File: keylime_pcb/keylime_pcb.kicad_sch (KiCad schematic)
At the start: 0 parts

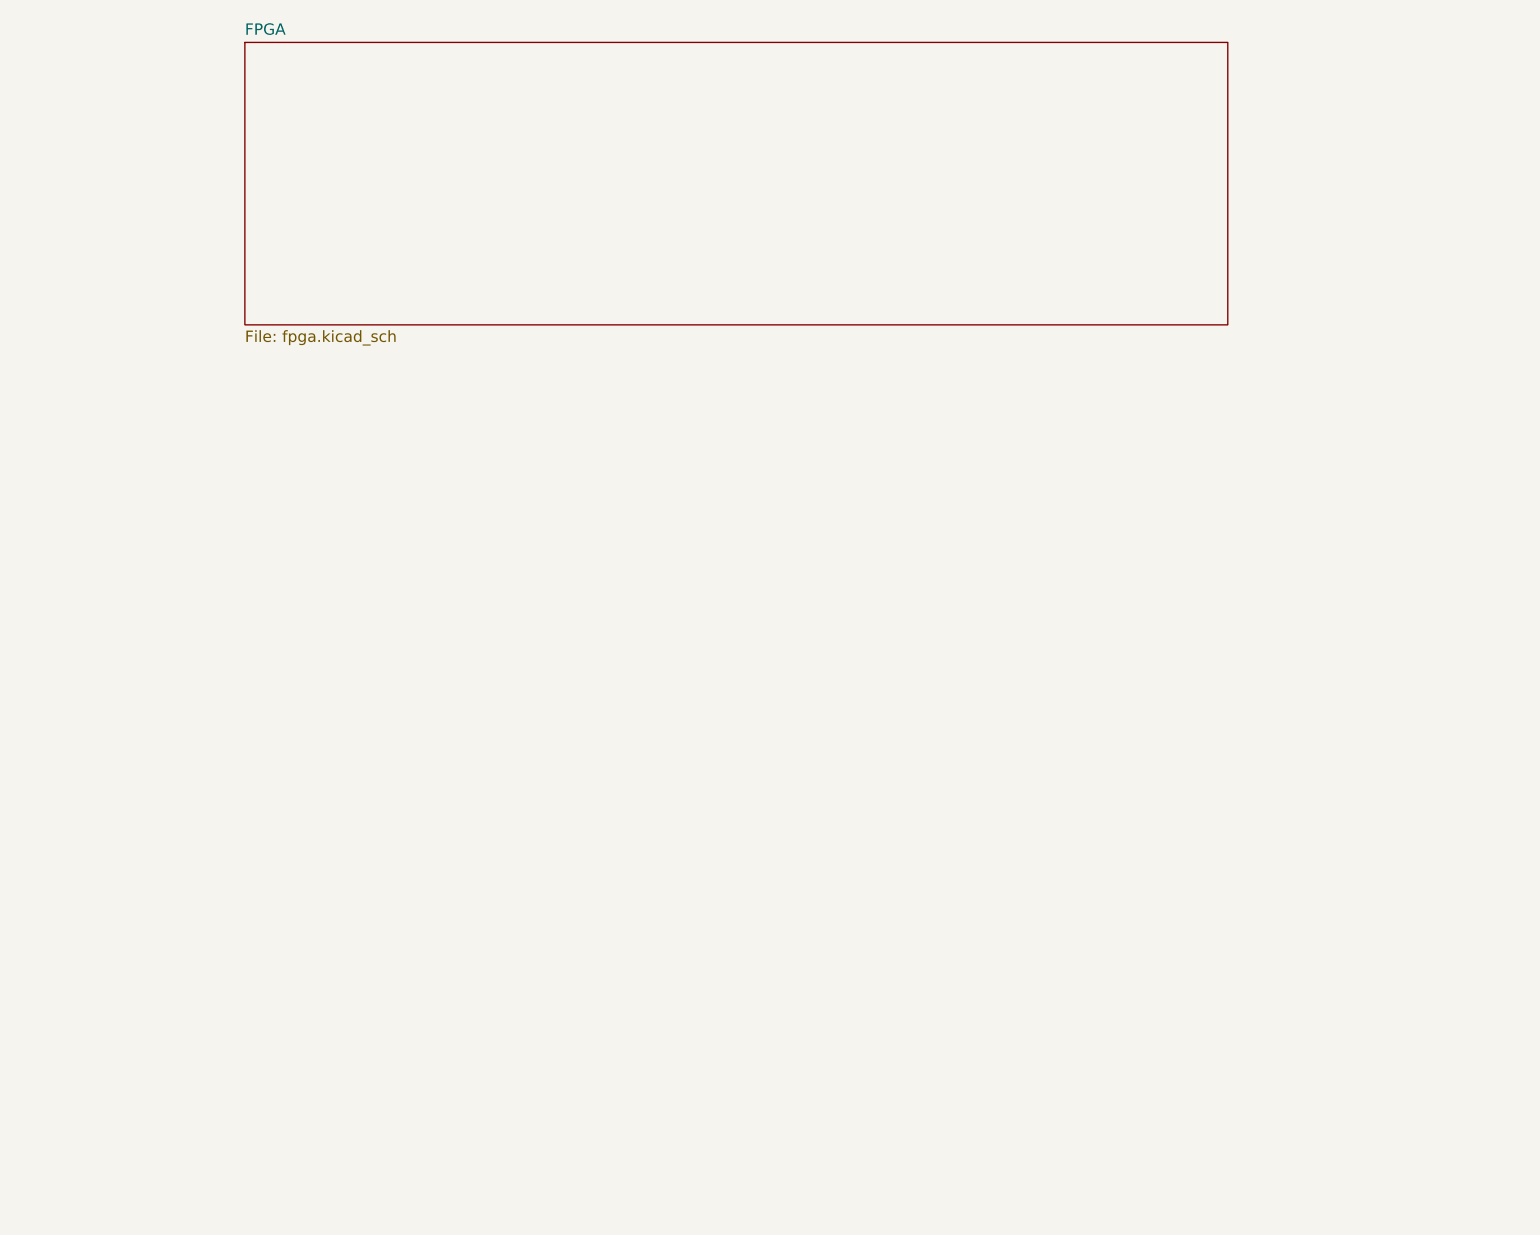
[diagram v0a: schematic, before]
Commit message: Finished adding most components.
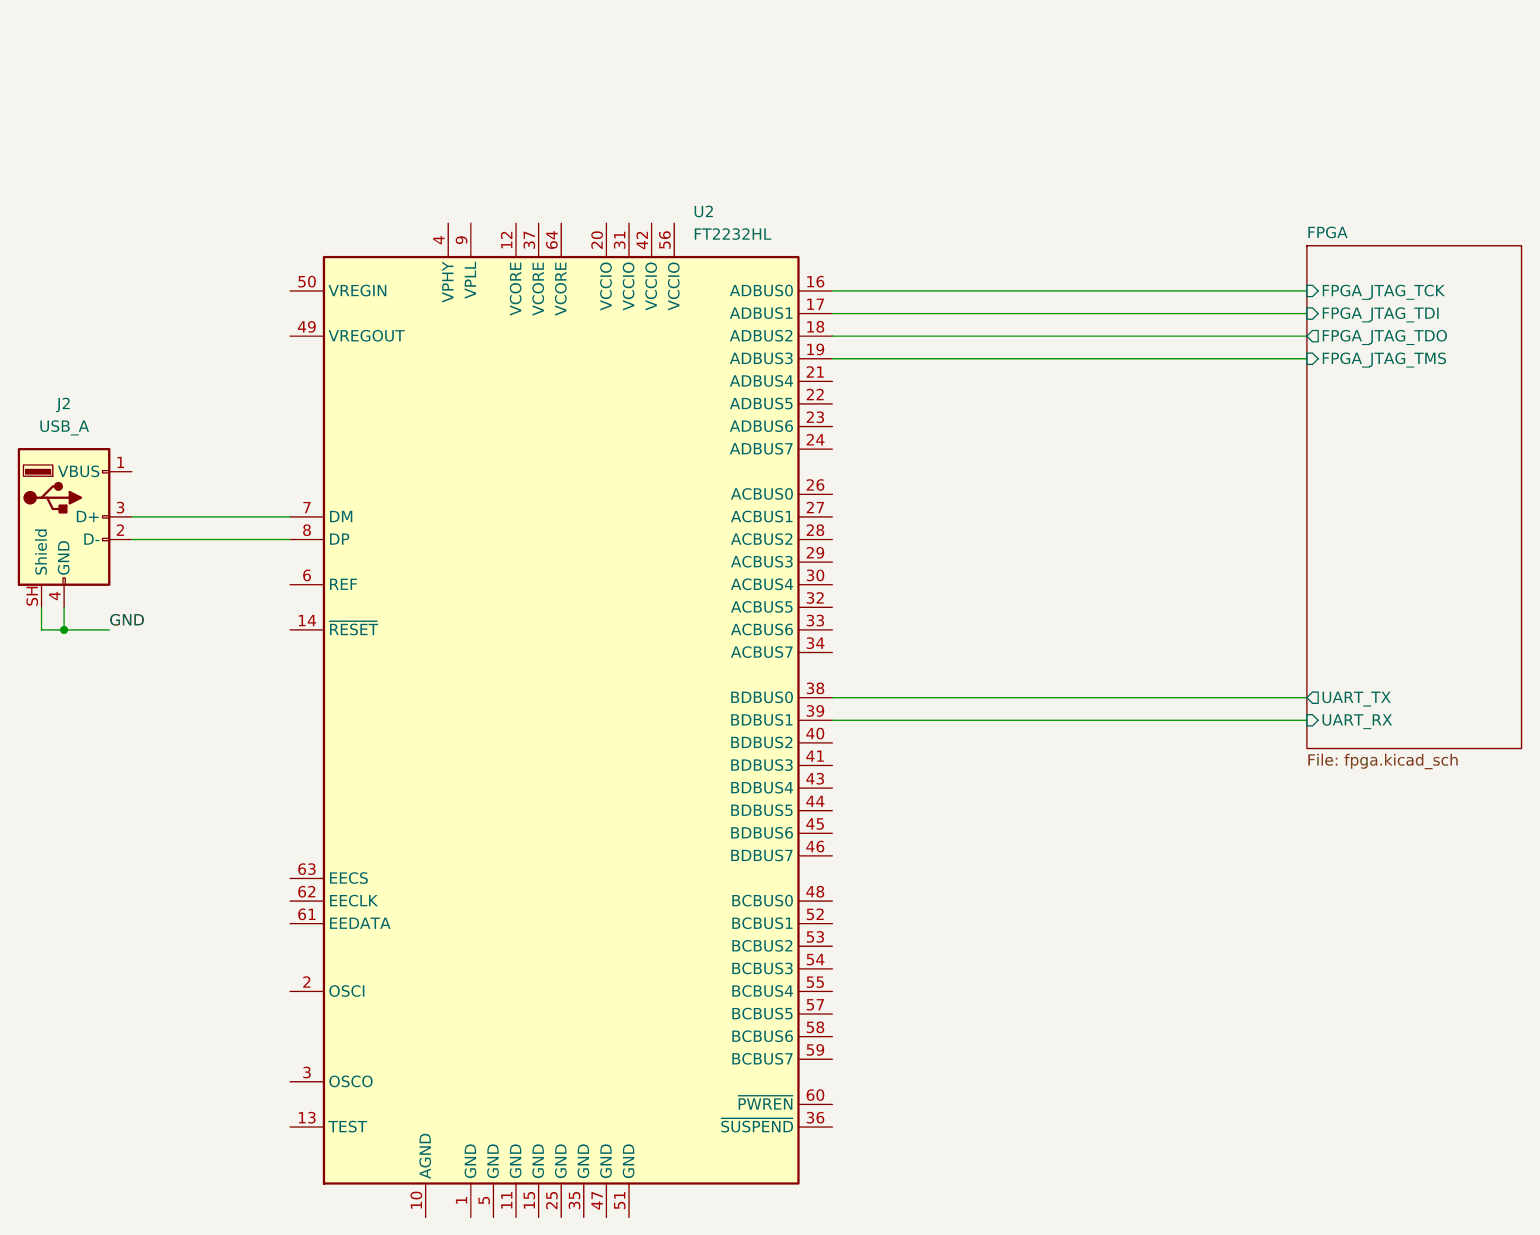
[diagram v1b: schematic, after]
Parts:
- added J2: USB_A, symbol Connector:USB_A
- added U2: FT2232HL, Package_QFP:LQFP-64_10x10mm_P0.5mm, symbol Interface_USB:FT2232HL
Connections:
- new net: J2.2 (D-), U2.8 (DP)
- new net: J2.3 (D+), U2.7 (DM)
- new net FPGA/FPGA_JTAG_TCK: U2.16 (ADBUS0)
- new net FPGA/FPGA_JTAG_TDI: U2.17 (ADBUS1)
- new net FPGA/FPGA_JTAG_TDO: U2.18 (ADBUS2)
- new net FPGA/FPGA_JTAG_TMS: U2.19 (ADBUS3)
- new net FPGA/UART_RX: U2.39 (BDBUS1)
- new net FPGA/UART_TX: U2.38 (BDBUS0)
- new net GND: J2.4 (GND), J2.SH (Shield)
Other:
- sheet FPGA ports: added FPGA_JTAG_TCK, FPGA_JTAG_TDI, FPGA_JTAG_TDO, FPGA_JTAG_TMS, UART_RX, UART_TX; removed none
